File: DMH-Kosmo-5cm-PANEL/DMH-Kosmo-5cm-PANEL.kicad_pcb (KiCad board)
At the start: 2 copper layers, 50 x 200 mm, 5 parts, among them J0 Panel_GND_Solder_Wire_Pad

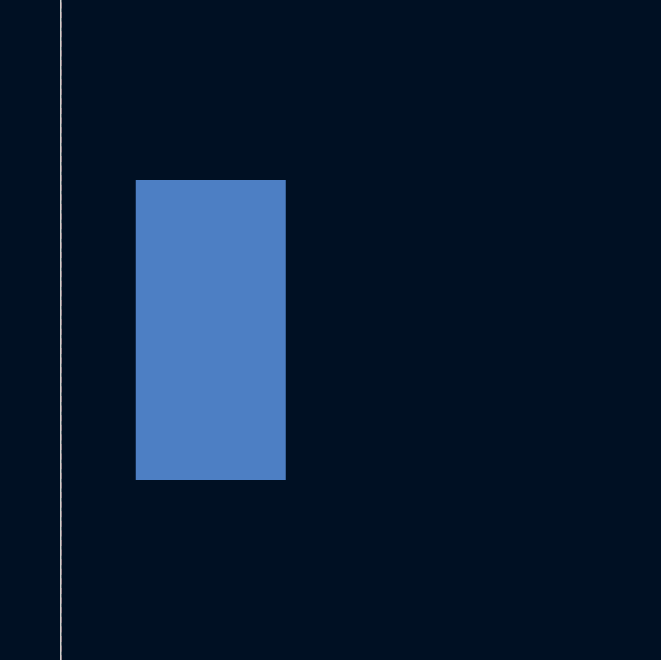
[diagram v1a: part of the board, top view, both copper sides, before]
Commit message: Matched main PCB size reference in PANEL templates
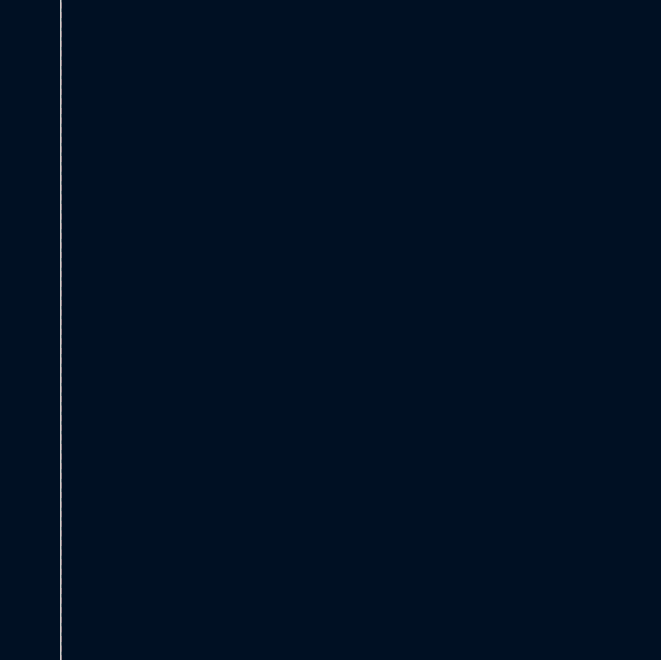
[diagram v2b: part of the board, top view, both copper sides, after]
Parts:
- removed J0: Panel_GND_Solder_Wire_Pad, SynthStuff:Panel_GND_SolderWirePad_5x10mm
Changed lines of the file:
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@@
 		)
 		(property ki_fp_filters "MountingHole*Pad*")
-		(sheetname "Root")
+		(sheetname "/")
 		(sheetfile "DMH-Kosmo-5cm-PANEL.kicad_sch")
-		(attr exclude_from_pos_files exclude_from_bom)
+		(units
+			(unit
+				(name "A")
+				(pins "1")
+			)
+		)
+		(attr exclude_from_bom)
 		(duplicate_pad_numbers_are_jumpers no)
 		(fp_circle
@@
 			(remove_unused_layers no)
 			(net "GND")
-			(pinfunction "1")
+			(pinfunction "1_1")
 			(pintype "input")
 			(zone_connect 2)
@@
 		)
 		(property ki_fp_filters "MountingHole*Pad*")
-		(sheetname "Root")
+		(sheetname "/")
 		(sheetfile "DMH-Kosmo-5cm-PANEL.kicad_sch")
-		(attr exclude_from_pos_files exclude_from_bom)
+		(units
+			(unit
+				(name "A")
+				(pins "1")
+			)
+		)
+		(attr exclude_from_bom)
 		(duplicate_pad_numbers_are_jumpers no)
 		(fp_circle
@@
 			(remove_unused_layers no)
 			(net "GND")
-			(pinfunction "1")
+			(pinfunction "1_1")
 			(pintype "input")
 			(zone_connect 2)
@@
 		)
 		(property ki_fp_filters "MountingHole*Pad*")
-		(sheetname "Root")
+		(sheetname "/")
 		(sheetfile "DMH-Kosmo-5cm-PANEL.kicad_sch")
-		(attr exclude_from_pos_files exclude_from_bom)
+		(units
+			(unit
+				(name "A")
+				(pins "1")
+			)
+		)
+		(attr exclude_from_bom)
 		(duplicate_pad_numbers_are_jumpers no)
 		(fp_circle
@@
 			(remove_unused_layers no)
 			(net "GND")
-			(pinfunction "1")
+			(pinfunction "1_1")
 			(pintype "input")
 			(zone_connect 2)
@@
 		)
 		(property ki_fp_filters "MountingHole*Pad*")
-		(sheetname "Root")
+		(sheetname "/")
 		(sheetfile "DMH-Kosmo-5cm-PANEL.kicad_sch")
-		(attr exclude_from_pos_files exclude_from_bom)
+		(units
+			(unit
+				(name "A")
+				(pins "1")
+			)
+		)
+		(attr exclude_from_bom)
 		(duplicate_pad_numbers_are_jumpers no)
 		(fp_circle
@@
 			(remove_unused_layers no)
 			(net "GND")
-			(pinfunction "1")
+			(pinfunction "1_1")
 			(pintype "input")
 			(zone_connect 2)
-		)
-		(embedded_fonts no)
-	)
-	(footprint "SynthStuff:Panel_GND_SolderWirePad_5x10mm"
-		(layer "B.Cu")
-		(at 55 130 180)
-		(descr "Wire Pad, Square, SMD Pad,  5mm x 10mm,")
-		(tags "MesurementPoint Square SMDPad 5mmx10mm ")
-		(property "Reference" "J0"
-			(at 0 3.81 0)
-			(layer "B.SilkS")
-			(hide yes)
-			(effects
-				(font
-					(size 1 1)
-					(thickness 0.15)
-				)
-				(justify mirror)
-			)
-		)
-		(property "Value" "Panel_GND_Solder_Wire_Pad"
-			(at 0 -6.35 0)
-			(layer "B.Fab")
-			(hide yes)
-			(effects
-				(font
-					(size 1 1)
-					(thickness 0.15)
-				)
-				(justify mirror)
-			)
-		)
-		(property "Datasheet" ""
-			(at 0 0 0)
-			(unlocked yes)
-			(layer "B.Fab")
-			(hide yes)
-			(effects
-				(font
-					(size 1.27 1.27)
-					(thickness 0.15)
-				)
-				(justify mirror)
-			)
-		)
-		(property "Description" "Solder pad to allow connection between PCB and Front Panel"
-			(at 0 0 0)
-			(unlocked yes)
-			(layer "B.Fab")
-			(hide yes)
-			(effects
-				(font
-					(size 1.27 1.27)
-					(thickness 0.15)
-				)
-				(justify mirror)
-			)
-		)
-		(property "Function" "GND"
-			(at 0 -6.75 0)
-			(layer "B.SilkS")
-			(effects
-				(font
-					(size 1.5 1.5)
-					(thickness 0.3)
-					(bold yes)
-				)
-				(justify mirror)
-			)
-		)
-		(property ki_fp_filters "Connector*:*_1x??_*")
-		(sheetname "Root")
-		(sheetfile "DMH-Kosmo-5cm-PANEL.kicad_sch")
-		(zone_connect 1)
-		(attr smd exclude_from_pos_files exclude_from_bom)
-		(duplicate_pad_numbers_are_jumpers no)
-		(fp_line
-			(start 2.75 5.25)
-			(end 2.75 -5.25)
-			(stroke
-				(width 0.05)
-				(type solid)
-			)
-			(layer "B.CrtYd")
-		)
-		(fp_line
-			(start 2.75 -5.25)
-			(end -2.75 -5.25)
-			(stroke
-				(width 0.05)
-				(type solid)
-			)
-			(layer "B.CrtYd")
-		)
-		(fp_line
-			(start -2.75 5.25)
-			(end 2.75 5.25)
-			(stroke
-				(width 0.05)
-				(type solid)
-			)
-			(layer "B.CrtYd")
-		)
-		(fp_line
-			(start -2.75 -5.25)
-			(end -2.75 5.25)
-			(stroke
-				(width 0.05)
-				(type solid)
-			)
-			(layer "B.CrtYd")
-		)
-		(fp_text user "${REFERENCE}"
-			(at 0 0 0)
-			(layer "B.Fab")
-			(effects
-				(font
-					(size 1 1)
-					(thickness 0.15)
-				)
-				(justify mirror)
-			)
-		)
-		(pad "1" smd rect
-			(at 0 0 180)
-			(size 5 10)
-			(layers "B.Cu" "B.Mask" "B.Paste")
-			(net "GND")
-			(pinfunction "Pin_1")
-			(pintype "power_out")
 		)
 		(embedded_fonts no)
@@
 	)
 	(gr_rect
-		(start 51 42.5)
-		(end 99 217.5)
+		(start 50.5 42.5)
+		(end 99.5 217.5)
 		(stroke
 			(width 0.05)
